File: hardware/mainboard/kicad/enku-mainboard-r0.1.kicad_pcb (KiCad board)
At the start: 4 copper layers, 54 x 94 mm, 122 parts, among them J1 1S LiPo + NTC, J2 Hirose DM3AT-SF-PEJM5, J3 FH34SRJ-24S-0.5SH(50), J5 GCT USB4105-GF-A-120, J6 4-pin pogo dock, J7 Tag-Connect TC2030-IDC-NL, Q1 IRLML6346TRPBF, SW1 HARD POWER, SW2 BOOT / RECOVERY, SW3 BTN_L1, SW4 BTN_L2, SW5 BTN_R1, SW6 BTN_R2, U1 ESP32-S3-WROOM-1-N16R8, U2 TPS2121, U3 BQ25185DLHR, U4 TPS63802DLAR, U5 BMI270, U6 DRV5032FBDBZR, U8 USBLC6-2SC6

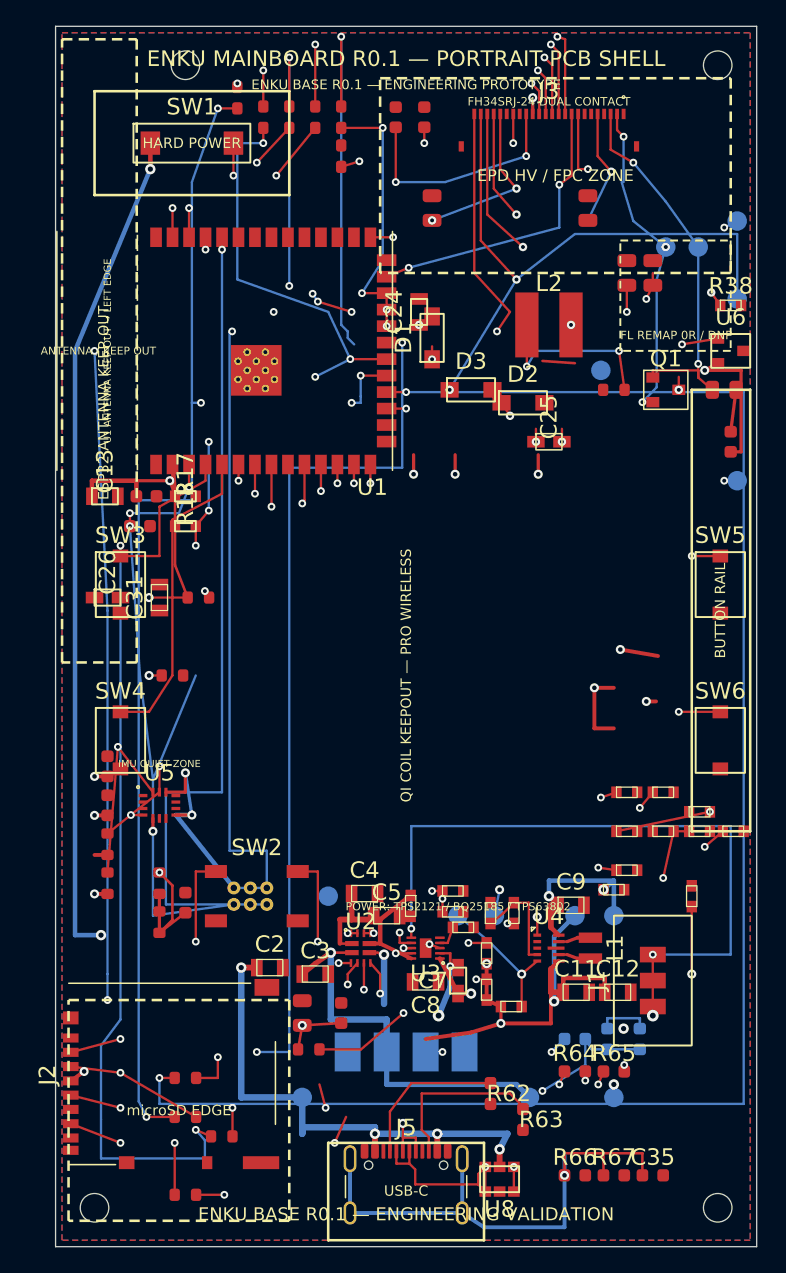
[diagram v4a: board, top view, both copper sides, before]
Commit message: pcb: move SD CS onto zero-crossing back-layer corridor
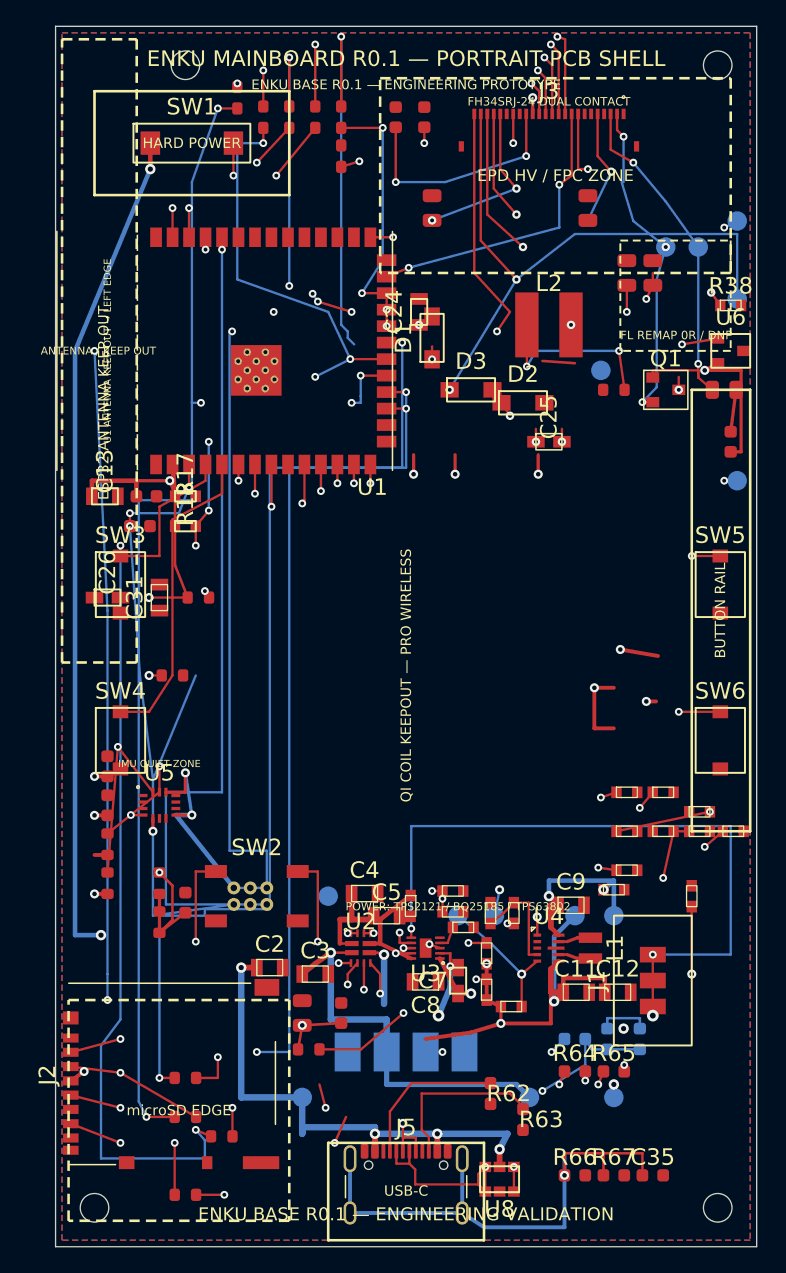
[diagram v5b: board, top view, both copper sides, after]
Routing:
- net SD_CS: track 130.5 -> 74.5 mm
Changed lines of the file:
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@@
   (segment (start 45.500 48.175) (end 47.000 48.175) (width 0.18) (layer "F.Cu") (net 60))
   (via (at 47.000 48.175) (size 0.60) (drill 0.30) (layers "F.Cu" "B.Cu") (net 60))
-  (segment (start 47.000 48.175) (end 73.000 48.175) (width 0.18) (layer "B.Cu") (net 60))
-  (segment (start 73.000 48.175) (end 73.000 103.000) (width 0.18) (layer "B.Cu") (net 60))
-  (segment (start 73.000 103.000) (end 28.000 103.000) (width 0.18) (layer "B.Cu") (net 60))
-  (segment (start 28.000 103.000) (end 28.000 101.000) (width 0.18) (layer "B.Cu") (net 60))
+  (segment (start 47.000 48.175) (end 47.000 54.000) (width 0.18) (layer "B.Cu") (net 60))
+  (segment (start 47.000 54.000) (end 36.500 54.000) (width 0.18) (layer "B.Cu") (net 60))
+  (segment (start 36.500 54.000) (end 36.500 88.000) (width 0.18) (layer "B.Cu") (net 60))
+  (segment (start 36.500 88.000) (end 31.500 88.000) (width 0.18) (layer "B.Cu") (net 60))
+  (segment (start 31.500 88.000) (end 31.500 88.500) (width 0.18) (layer "B.Cu") (net 60))
+  (segment (start 31.500 88.500) (end 28.000 88.500) (width 0.18) (layer "B.Cu") (net 60))
+  (segment (start 28.000 88.500) (end 28.000 101.000) (width 0.18) (layer "B.Cu") (net 60))
   (via (at 28.000 101.000) (size 0.60) (drill 0.30) (layers "F.Cu" "B.Cu") (net 60))
   (segment (start 28.000 101.000) (end 29.175 101.000) (width 0.18) (layer "F.Cu") (net 60))

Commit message: pcb: route SD CS across clean three-layer corridor
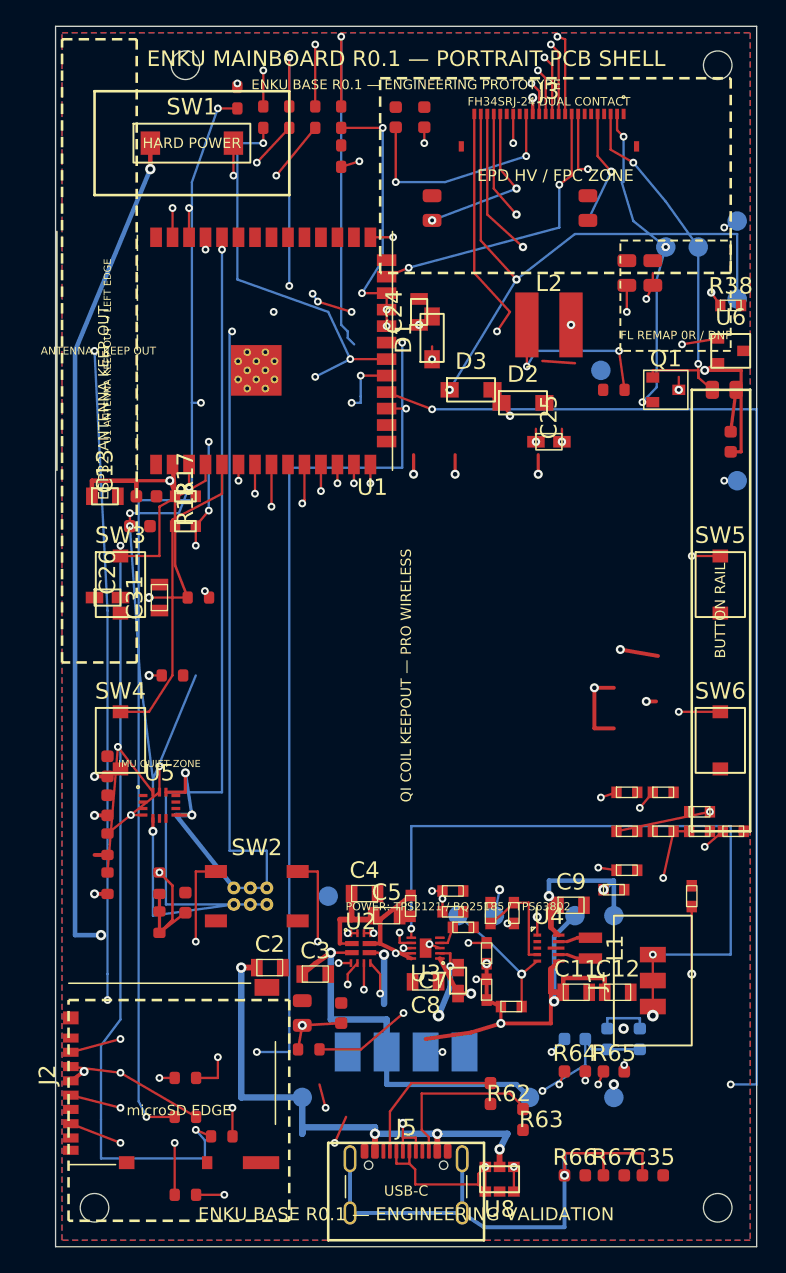
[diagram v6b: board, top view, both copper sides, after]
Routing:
- net SD_CS: track 74.5 -> 128.4 mm, vias 2 -> 3
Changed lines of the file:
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@@
   (via (at 25.800 80.750) (size 0.60) (drill 0.30) (layers "F.Cu" "In2.Cu") (net 55))
   (segment (start 25.800 80.750) (end 26.7375 80.7500) (width 0.18) (layer "F.Cu") (net 55))
-  (segment (start 45.500 48.175) (end 47.000 48.175) (width 0.18) (layer "F.Cu") (net 60))
-  (via (at 47.000 48.175) (size 0.60) (drill 0.30) (layers "F.Cu" "B.Cu") (net 60))
-  (segment (start 47.000 48.175) (end 47.000 54.000) (width 0.18) (layer "B.Cu") (net 60))
-  (segment (start 47.000 54.000) (end 36.500 54.000) (width 0.18) (layer "B.Cu") (net 60))
-  (segment (start 36.500 54.000) (end 36.500 88.000) (width 0.18) (layer "B.Cu") (net 60))
-  (segment (start 36.500 88.000) (end 31.500 88.000) (width 0.18) (layer "B.Cu") (net 60))
-  (segment (start 31.500 88.000) (end 31.500 88.500) (width 0.18) (layer "B.Cu") (net 60))
-  (segment (start 31.500 88.500) (end 28.000 88.500) (width 0.18) (layer "B.Cu") (net 60))
-  (segment (start 28.000 88.500) (end 28.000 101.000) (width 0.18) (layer "B.Cu") (net 60))
-  (via (at 28.000 101.000) (size 0.60) (drill 0.30) (layers "F.Cu" "B.Cu") (net 60))
+  (segment (start 45.500 48.175) (end 49.000 49.500) (width 0.18) (layer "F.Cu") (net 60))
+  (via (at 49.000 49.500) (size 0.60) (drill 0.30) (layers "F.Cu" "B.Cu") (net 60))
+  (segment (start 49.000 49.500) (end 74.000 49.500) (width 0.18) (layer "B.Cu") (net 60))
+  (segment (start 74.000 49.500) (end 74.000 101.500) (width 0.18) (layer "B.Cu") (net 60))
+  (segment (start 74.000 101.500) (end 72.000 101.500) (width 0.18) (layer "B.Cu") (net 60))
+  (via (at 72.000 101.500) (size 0.60) (drill 0.30) (layers "B.Cu" "In1.Cu") (net 60))
+  (segment (start 72.000 101.500) (end 28.000 101.500) (width 0.18) (layer "In1.Cu") (net 60))
+  (segment (start 28.000 101.500) (end 28.000 101.000) (width 0.18) (layer "In1.Cu") (net 60))
+  (via (at 28.000 101.000) (size 0.60) (drill 0.30) (layers "F.Cu" "In1.Cu") (net 60))
   (segment (start 28.000 101.000) (end 29.175 101.000) (width 0.18) (layer "F.Cu") (net 60))
   (segment (start 41.71 53.75) (end 41.71 55.20) (width 0.18) (layer "F.Cu") (net 56))

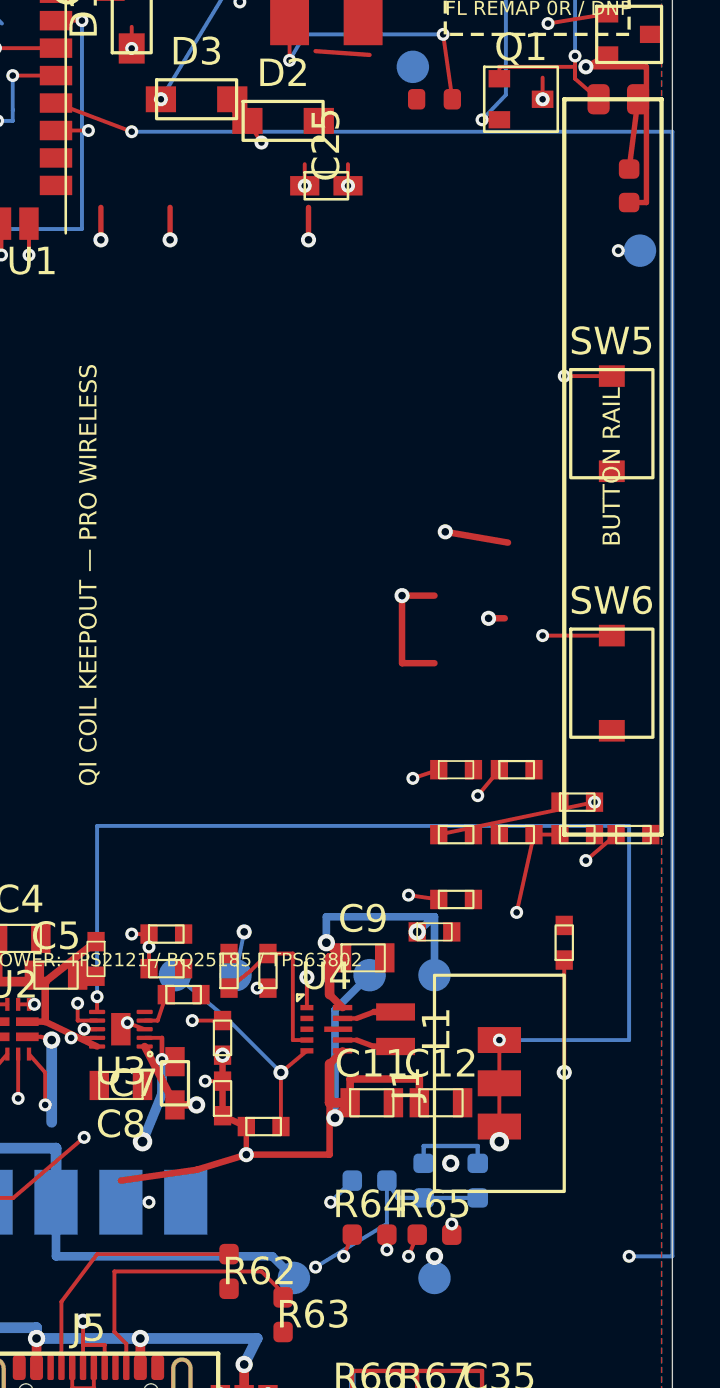
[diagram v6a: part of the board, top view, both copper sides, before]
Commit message: pcb: pull SD CS corridor inside board edge
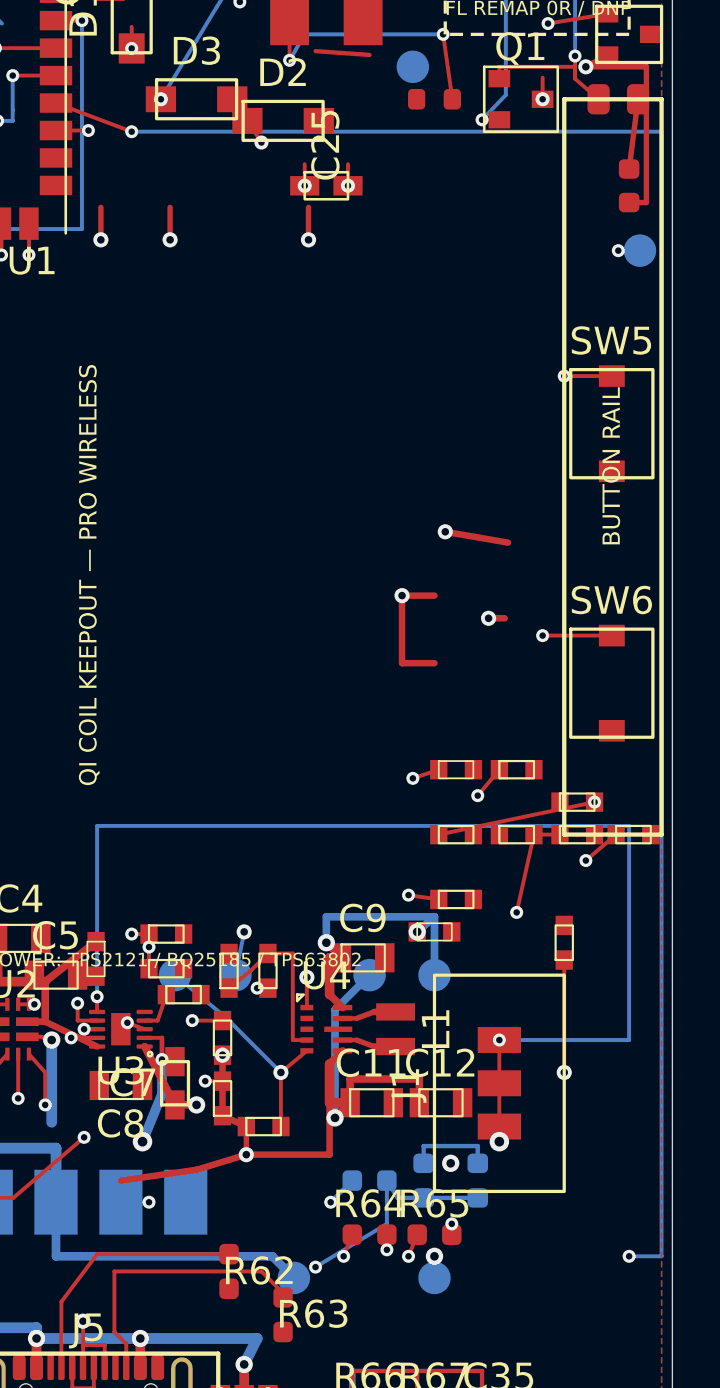
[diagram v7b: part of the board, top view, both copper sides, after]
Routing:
- net SD_CS: track 128.4 -> 127.4 mm
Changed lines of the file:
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@@
   (segment (start 45.500 48.175) (end 49.000 49.500) (width 0.18) (layer "F.Cu") (net 60))
   (via (at 49.000 49.500) (size 0.60) (drill 0.30) (layers "F.Cu" "B.Cu") (net 60))
-  (segment (start 49.000 49.500) (end 74.000 49.500) (width 0.18) (layer "B.Cu") (net 60))
-  (segment (start 74.000 49.500) (end 74.000 101.500) (width 0.18) (layer "B.Cu") (net 60))
-  (segment (start 74.000 101.500) (end 72.000 101.500) (width 0.18) (layer "B.Cu") (net 60))
+  (segment (start 49.000 49.500) (end 73.500 49.500) (width 0.18) (layer "B.Cu") (net 60))
+  (segment (start 73.500 49.500) (end 73.500 101.500) (width 0.18) (layer "B.Cu") (net 60))
+  (segment (start 73.500 101.500) (end 72.000 101.500) (width 0.18) (layer "B.Cu") (net 60))
   (via (at 72.000 101.500) (size 0.60) (drill 0.30) (layers "B.Cu" "In1.Cu") (net 60))
   (segment (start 72.000 101.500) (end 28.000 101.500) (width 0.18) (layer "In1.Cu") (net 60))

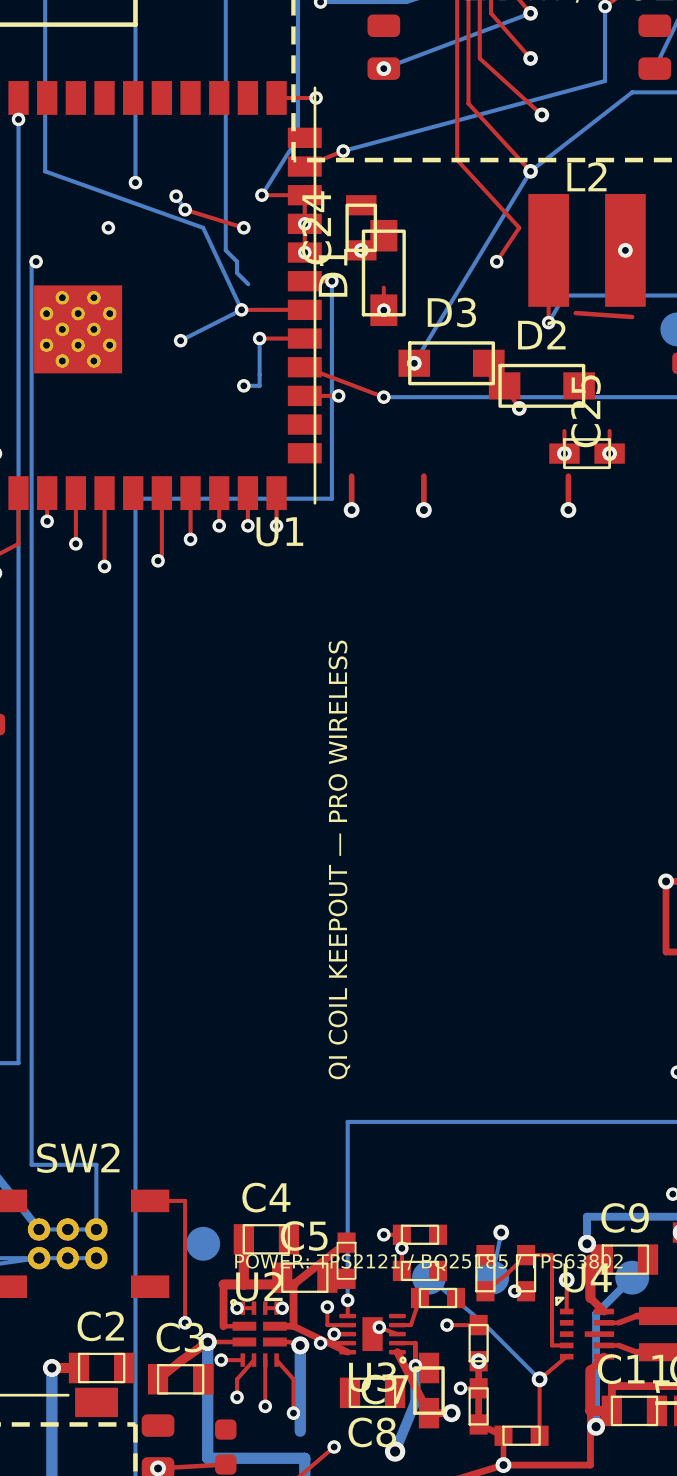
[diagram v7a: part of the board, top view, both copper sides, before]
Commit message: pcb: correct EPD and charger signal escapes
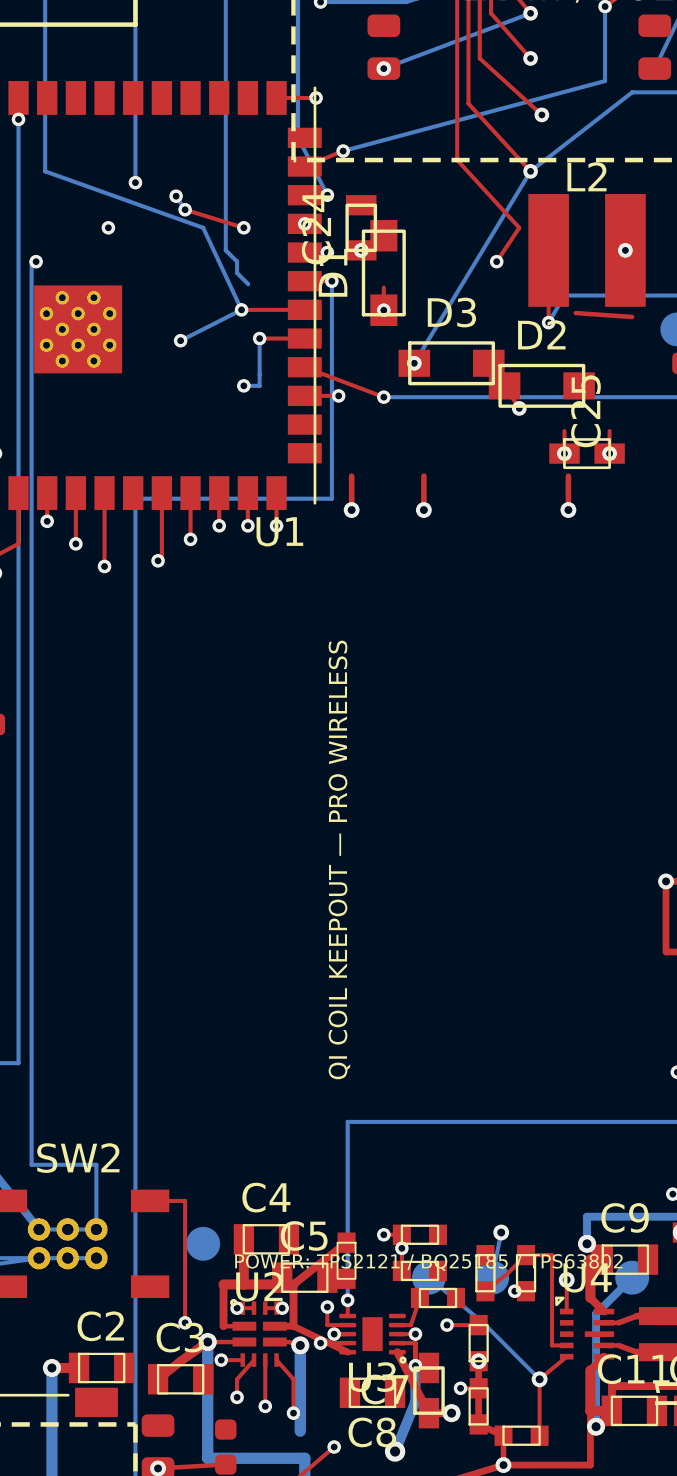
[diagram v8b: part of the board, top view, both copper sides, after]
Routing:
- net CHG_STAT2: track 6.15 -> 4.72 mm
- net EPD_RST: track 18.3 -> 17.2 mm
- net EPD_DC: track 19.1 -> 18.1 mm
- net EPD_CS: track 20.8 -> 21.7 mm
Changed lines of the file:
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@@
   (via (at 45.2 27.825) (size 0.60) (drill 0.30) (layers "F.Cu" "B.Cu") (net 66))
   (segment (start 45.2 27.825) (end 45.2 38.0) (width 0.18) (layer "B.Cu") (net 66))
-  (segment (start 45.2 38.0) (end 43.6 40.555) (width 0.18) (layer "B.Cu") (net 66))
-  (via (at 43.6 40.555) (size 0.60) (drill 0.30) (layers "F.Cu" "B.Cu") (net 66))
-  (segment (start 43.6 40.555) (end 45.5 40.555) (width 0.18) (layer "F.Cu") (net 66))
+  (segment (start 45.200 38.000) (end 46.500 40.555) (width 0.18) (layer "B.Cu") (net 66))
+  (via (at 46.500 40.555) (size 0.60) (drill 0.30) (layers "F.Cu" "B.Cu") (net 66))
+  (segment (start 46.500 40.555) (end 45.500 40.555) (width 0.18) (layer "F.Cu") (net 66))
   (segment (start 43.525 98.8) (end 46.8 96.0) (width 0.18) (layer "F.Cu") (net 9))
   (segment (start 46.8 96.0) (end 46.8 94.8) (width 0.18) (layer "In1.Cu") (net 9))
@@
   (via (at 35.5 30.5) (size 0.60) (drill 0.30) (layers "F.Cu" "In1.Cu") (net 64))
   (segment (start 35.5 30.5) (end 43.5 41.5) (width 0.18) (layer "In1.Cu") (net 64))
-  (segment (start 43.5 41.5) (end 45.5 43.095) (width 0.18) (layer "In1.Cu") (net 64))
-  (via (at 45.5 43.095) (size 0.60) (drill 0.30) (layers "F.Cu" "In1.Cu") (net 64))
+  (segment (start 43.500 41.500) (end 46.500 43.095) (width 0.18) (layer "In1.Cu") (net 64))
+  (via (at 46.500 43.095) (size 0.60) (drill 0.30) (layers "F.Cu" "In1.Cu") (net 64))
+  (segment (start 46.500 43.095) (end 45.500 43.095) (width 0.18) (layer "F.Cu") (net 64))
   (segment (start 40 27.825) (end 37.0 31.5) (width 0.18) (layer "F.Cu") (net 65))
   (via (at 37.0 31.5) (size 0.60) (drill 0.30) (layers "F.Cu" "In2.Cu") (net 65))
@@
   (via (at 51.8 90.6) (size 0.60) (drill 0.30) (layers "F.Cu" "In2.Cu") (net 52))
   (segment (start 51.8 90.6) (end 53.2 90.6) (width 0.18) (layer "F.Cu") (net 52))
-  (segment (start 49.6 91.0) (end 48.8 90.7) (width 0.18) (layer "F.Cu") (net 93))
-  (via (at 48.8 90.7) (size 0.60) (drill 0.30) (layers "F.Cu" "In1.Cu") (net 93))
-  (segment (start 48.8 90.7) (end 52.4 93.4) (width 0.18) (layer "In1.Cu") (net 93))
+  (segment (start 49.600 91.000) (end 50.400 91.000) (width 0.18) (layer "F.Cu") (net 93))
+  (via (at 50.400 91.000) (size 0.60) (drill 0.30) (layers "F.Cu" "In1.Cu") (net 93))
+  (segment (start 50.400 91.000) (end 52.400 93.400) (width 0.18) (layer "In1.Cu") (net 93))
   (via (at 52.4 93.4) (size 0.60) (drill 0.30) (layers "F.Cu" "In1.Cu") (net 93))
   (segment (start 52.4 93.4) (end 53.2 93.4) (width 0.18) (layer "F.Cu") (net 93))
@@
   (segment (start 49.000 45.650) (end 49.000 44.650) (width 0.18) (layer "F.Cu") (net 30))
   (segment (start 59.000 52.000) (end 59.000 51.000) (width 0.18) (layer "F.Cu") (net 31))
-  (segment (start 45.500 43.095) (end 45.500 42.095) (width 0.18) (layer "F.Cu") (net 64))
-  (segment (start 45.500 41.825) (end 45.500 40.825) (width 0.18) (layer "F.Cu") (net 65))
   (segment (start 33.625 103.300) (end 40.800 103.300) (width 0.18) (layer "In1.Cu") (net 11))
   (segment (start 29.175 106.000) (end 41.500 106.000) (width 0.18) (layer "In1.Cu") (net 12))
